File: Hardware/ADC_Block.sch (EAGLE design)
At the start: 28 parts, among them U1 ADS1015, U2 PCA9306

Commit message: Added DCIN pin Renamed boards and moved name around clenaed up copper pours clenaed up dimensions and units.
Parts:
- R4, R5: value 2.2k -> DNP
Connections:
- new net DCIN: U$2.DCIN, U$3.DCIN
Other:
- note added: "v02"
- note removed: "01"
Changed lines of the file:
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@@
 <part name="SUPPLY4" library="SparkFun-Aesthetics" deviceset="1.8V" device=""/>
 <part name="R3" library="SparkFun-Resistors" deviceset="200KOHM1/10W1%(0603)" device="200K" value="200k"/>
-<part name="R4" library="SparkFun-Resistors" deviceset="2.2KOHM1/10W1%(0603)" device="" value="2.2k"/>
-<part name="R5" library="SparkFun-Resistors" deviceset="2.2KOHM1/10W1%(0603)" device="" value="2.2k"/>
+<part name="R4" library="SparkFun-Resistors" deviceset="2.2KOHM1/10W1%(0603)" device="" value="DNP"/>
+<part name="R5" library="SparkFun-Resistors" deviceset="2.2KOHM1/10W1%(0603)" device="" value="DNP"/>
 <part name="GND2" library="SparkFun-Aesthetics" deviceset="GND" device=""/>
 <part name="GND5" library="SparkFun-Aesthetics" deviceset="GND" device=""/>
@@
 1001010 (0x74)
 1001011 (0x75)</text>
-<text x="237.744" y="6.604" size="3.81" layer="95">01</text>
+<text x="237.744" y="6.604" size="2.54" layer="94">v02</text>
 <text x="165.1" y="7.62" size="3.81" layer="95">M Hord</text>
 </plain>
@@
 </segment>
 </net>
+<net name="DCIN" class="0">
+<segment>
+<pinref part="U$3" gate="G$1" pin="DCIN"/>
+<wire x1="172.72" y1="152.4" x2="170.18" y2="152.4" width="0.1524" layer="91"/>
+<label x="170.18" y="152.4" size="1.27" layer="95" rot="R180" xref="yes"/>
+</segment>
+<segment>
+<pinref part="U$2" gate="G$1" pin="DCIN"/>
+<wire x1="25.4" y1="152.4" x2="22.86" y2="152.4" width="0.1524" layer="91"/>
+<label x="22.86" y="152.4" size="1.27" layer="95" rot="R180" xref="yes"/>
+</segment>
+</net>

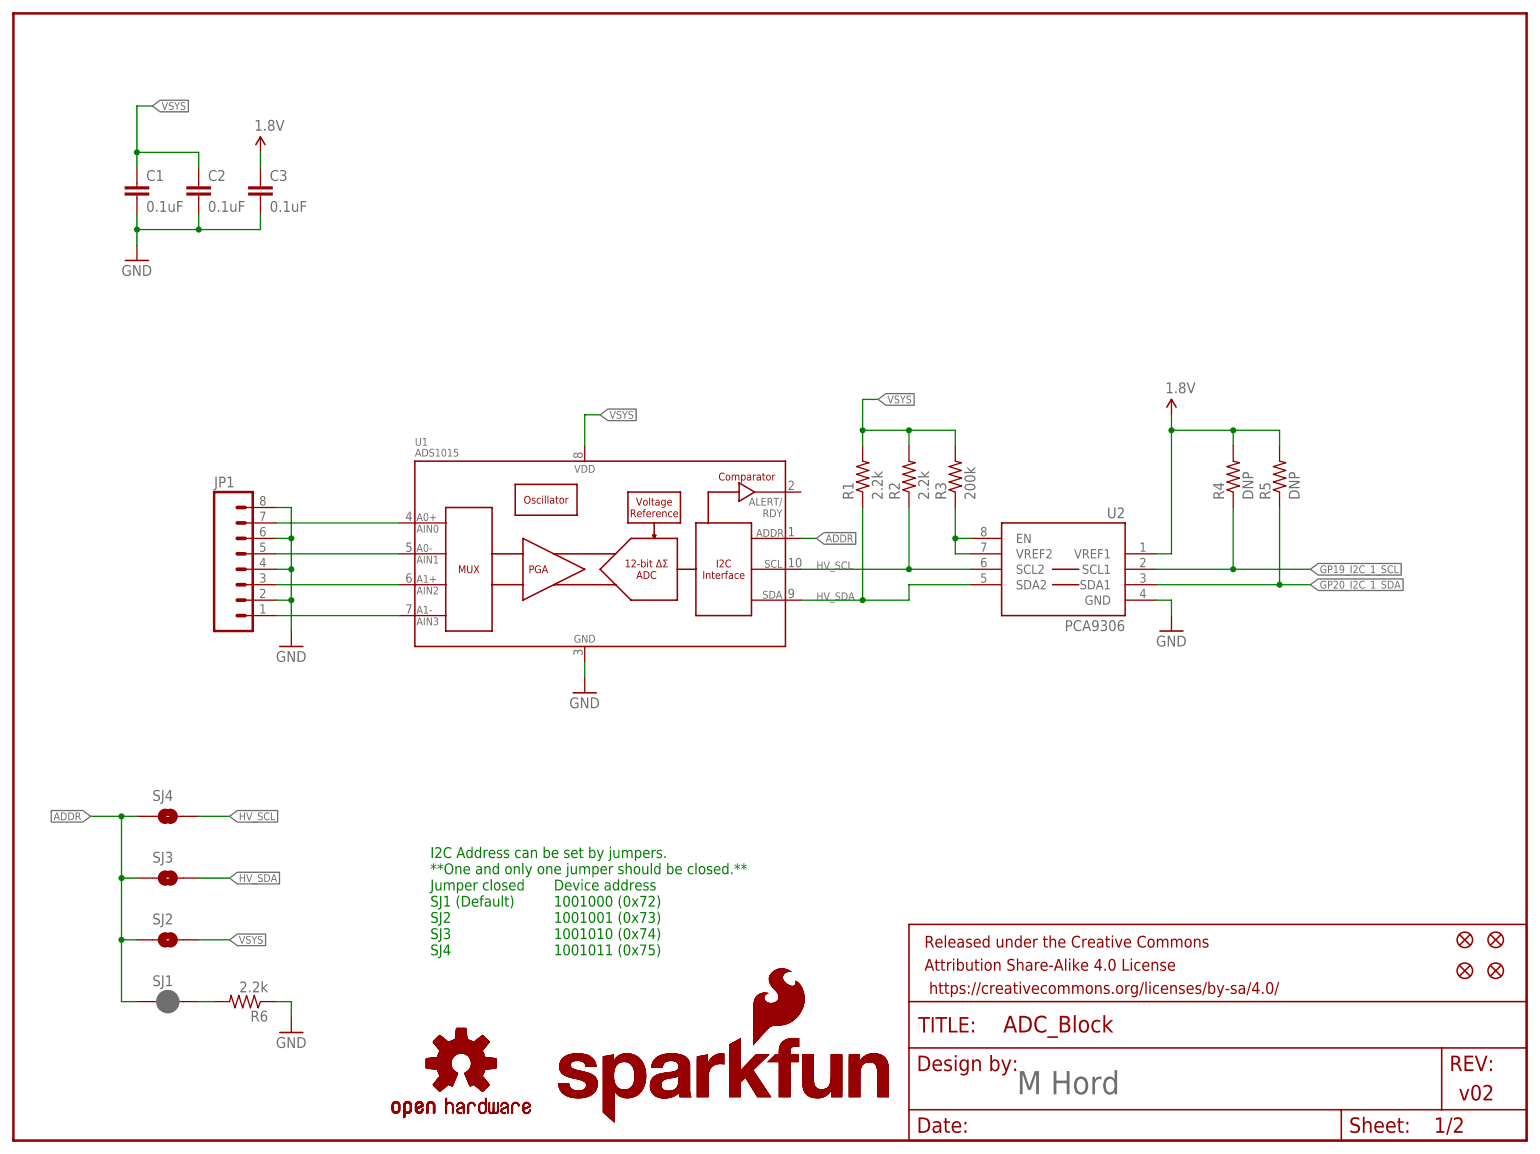
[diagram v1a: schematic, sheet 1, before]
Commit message: Chg pullups to 10k, update gnd and pwr traces, rev to 10
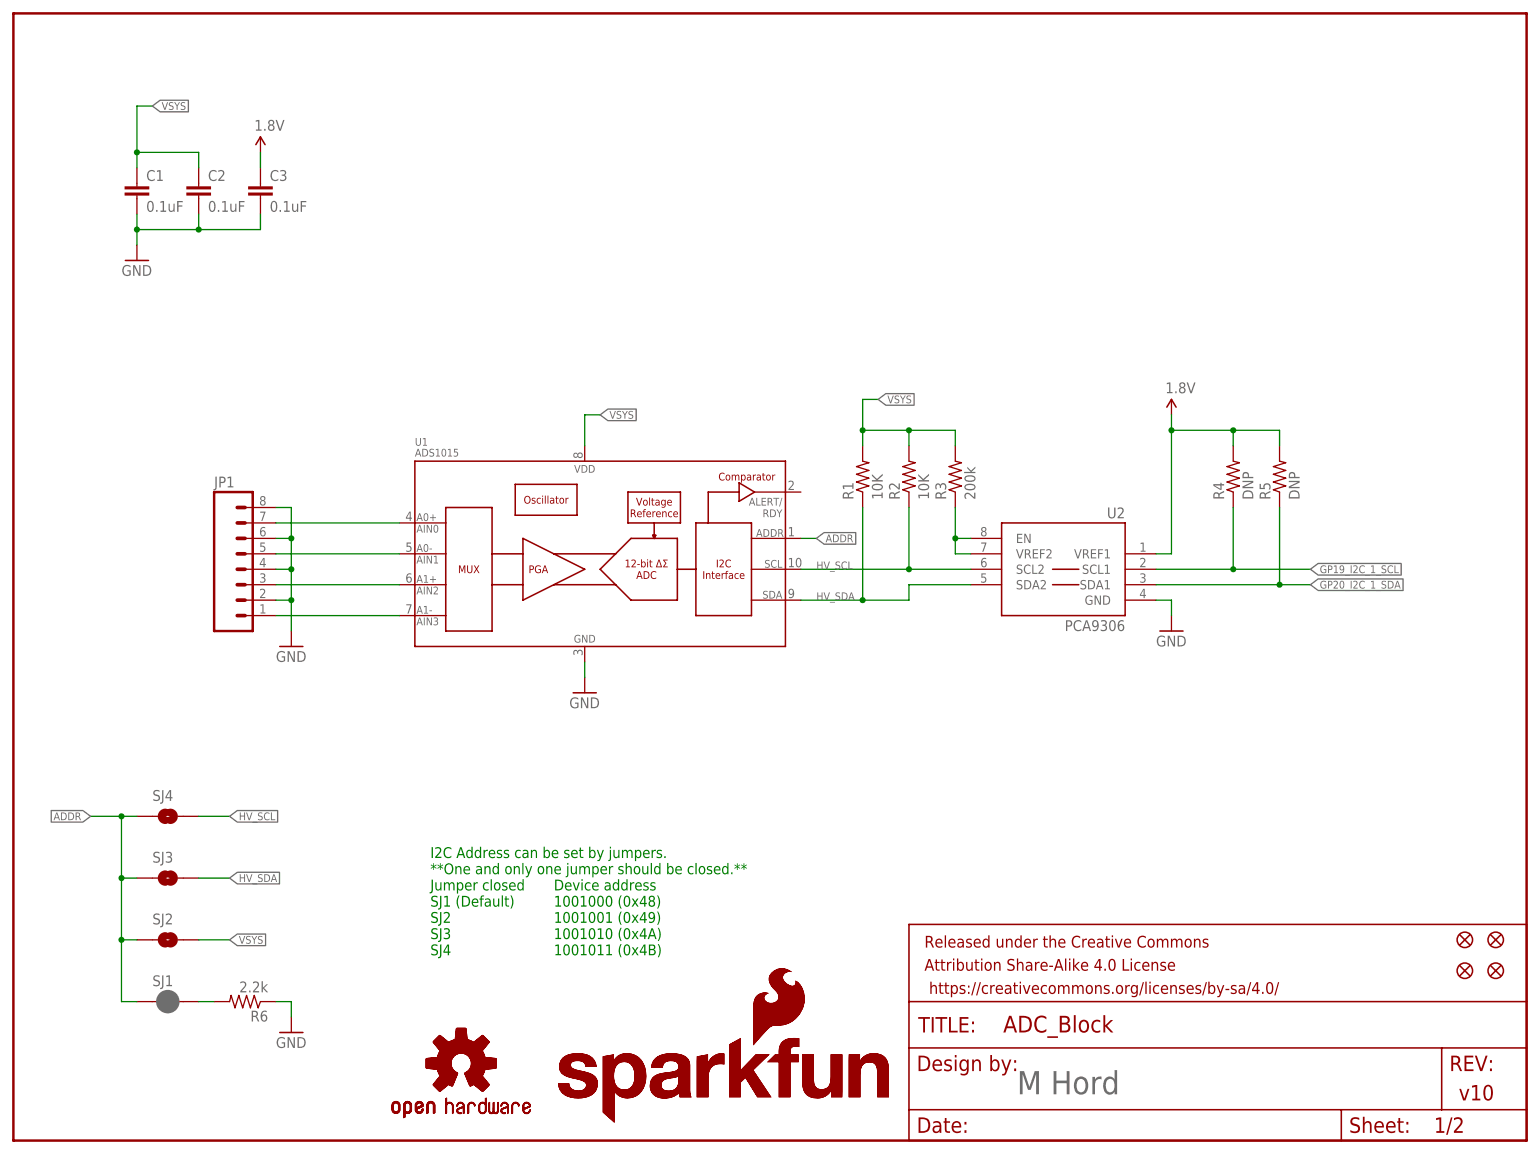
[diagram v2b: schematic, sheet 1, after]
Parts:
- R1, R2: value 2.2k -> 10K; device SparkFun-Resistors:2.2KOHM1/10W1%(0603) -> SparkFun-Resistors:10KOHM1/10W1%(0603)0603
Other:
- note added: "Device address 1001000 (0x48) 1001001 (0x49) 1001010 (0x4A) 1001011 (0x4B)"
- note added: "v10"
- note removed: "Device address 1001000 (0x72) 1001001 (0x73) 1001010 (0x74) 1001011 (0x75)"
- note removed: "v02"
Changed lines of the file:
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@@
 <?xml version="1.0" encoding="utf-8"?>
 <!DOCTYPE eagle SYSTEM "eagle.dtd">
-<eagle version="6.5.0">
+<eagle version="6.6.0">
 <drawing>
 <settings>
@@
 <layer number="254" name="cooling" color="7" fill="1" visible="yes" active="yes"/>
 </layers>
-<schematic xreflabel="%F%N/%S" xrefpart="1_/%S.%C%R">
+<schematic xreflabel="%F%N/%S" xrefpart="/%S.%C%R">
 <attributes>
 </attributes>
@@
 <part name="C1" library="SparkFun-Capacitors" deviceset="0.1UF-25V(+80/-20%)(0603)" device="" value="0.1uF"/>
 <part name="U1" library="SparkFun-AnalogIC" deviceset="ADS1015" device="" value="ADS1015"/>
-<part name="R1" library="SparkFun-Resistors" deviceset="2.2KOHM1/10W1%(0603)" device="" value="2.2k"/>
-<part name="R2" library="SparkFun-Resistors" deviceset="2.2KOHM1/10W1%(0603)" device="" value="2.2k"/>
+<part name="R1" library="SparkFun-Resistors" deviceset="10KOHM1/10W1%(0603)" device="0603" value="10K"/>
+<part name="R2" library="SparkFun-Resistors" deviceset="10KOHM1/10W1%(0603)" device="0603" value="10K"/>
 <part name="U2" library="SparkFun-DigitalIC" deviceset="PCA9306" device="PCA9306DC-1:1" value="PCA9306"/>
 <part name="SUPPLY1" library="SparkFun-Aesthetics" deviceset="1.8V" device=""/>
@@
 SJ4</text>
 <text x="88.9" y="30.48" size="1.778" layer="91">Device address
-1001000 (0x72)
-1001001 (0x73)
-1001010 (0x74)
-1001011 (0x75)</text>
-<text x="237.744" y="6.604" size="2.54" layer="94">v02</text>
+1001000 (0x48)
+1001001 (0x49)
+1001010 (0x4A)
+1001011 (0x4B)</text>
+<text x="237.744" y="6.604" size="2.54" layer="94">v10</text>
 <text x="165.1" y="7.62" size="3.81" layer="95">M Hord</text>
 </plain>

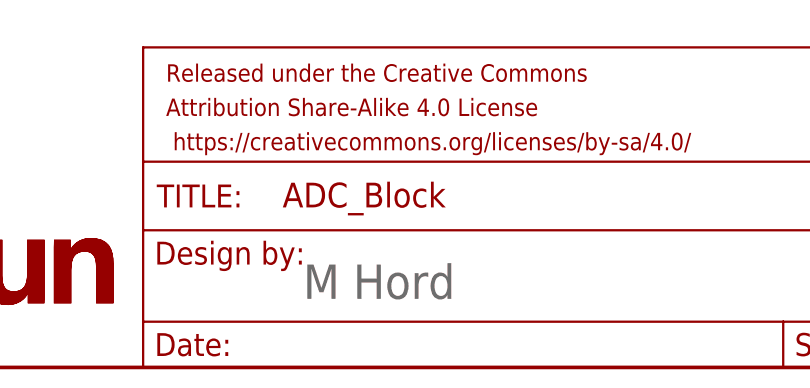
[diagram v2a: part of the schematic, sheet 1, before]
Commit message: Rev to 10, fix pwr, gnd, txt
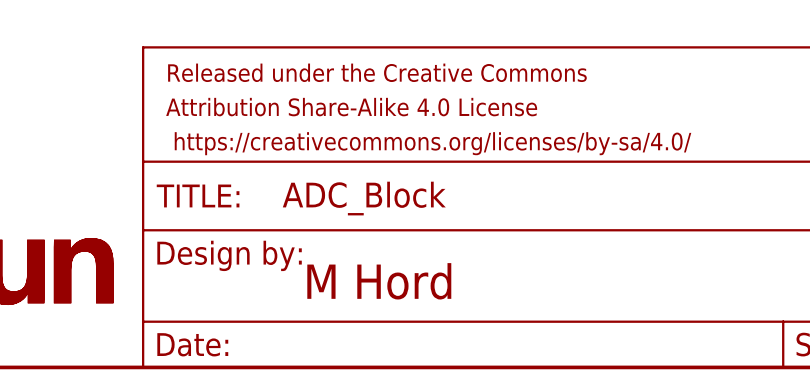
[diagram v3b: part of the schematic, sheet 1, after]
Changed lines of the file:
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@@
 1001011 (0x4B)</text>
 <text x="237.744" y="6.604" size="2.54" layer="94">v10</text>
-<text x="165.1" y="7.62" size="3.81" layer="95">M Hord</text>
+<text x="165.1" y="7.62" size="3.81" layer="94">M Hord</text>
 </plain>
 <instances>
